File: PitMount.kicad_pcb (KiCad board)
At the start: 2 copper layers, 27 x 30 mm, 16 parts, among them J1 Conn_01x07, Q1 BC817, Q2 IRLML6401, U1 UnifyNano, U2 ELRS-Rx

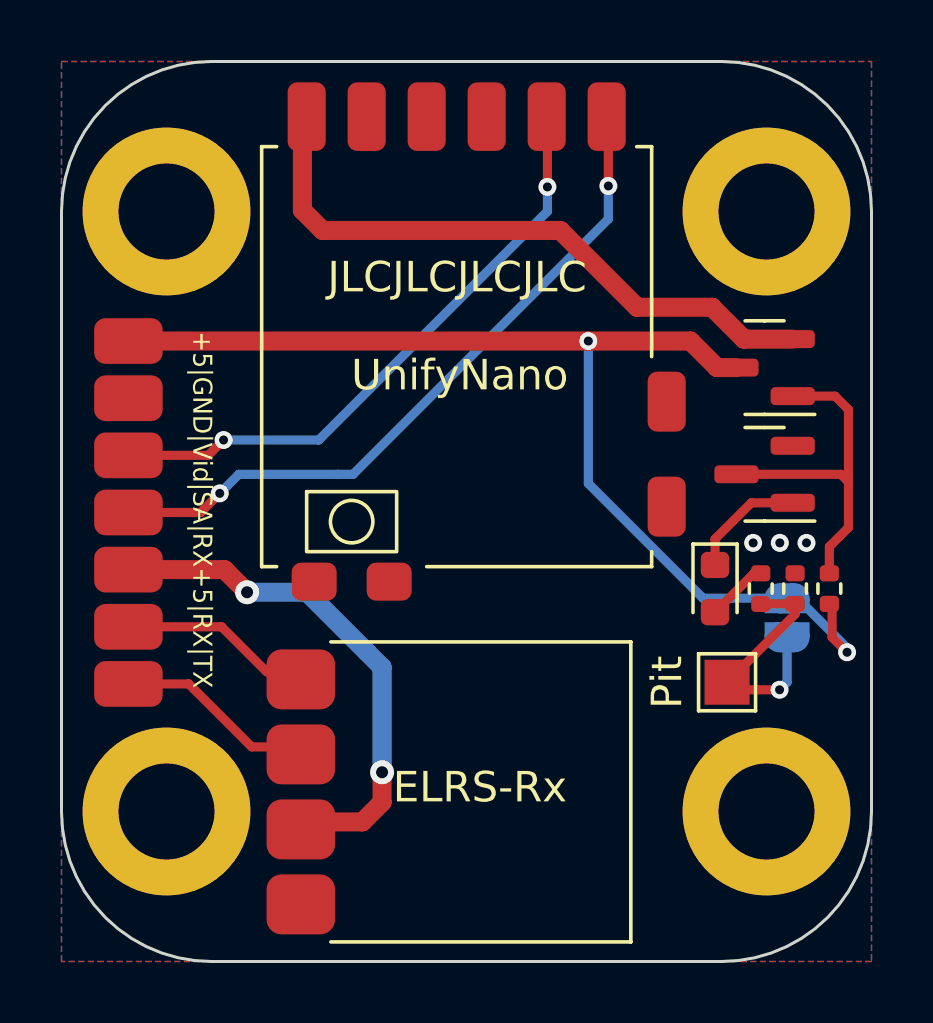
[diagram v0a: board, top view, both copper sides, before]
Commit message: Update PCB with new footprints
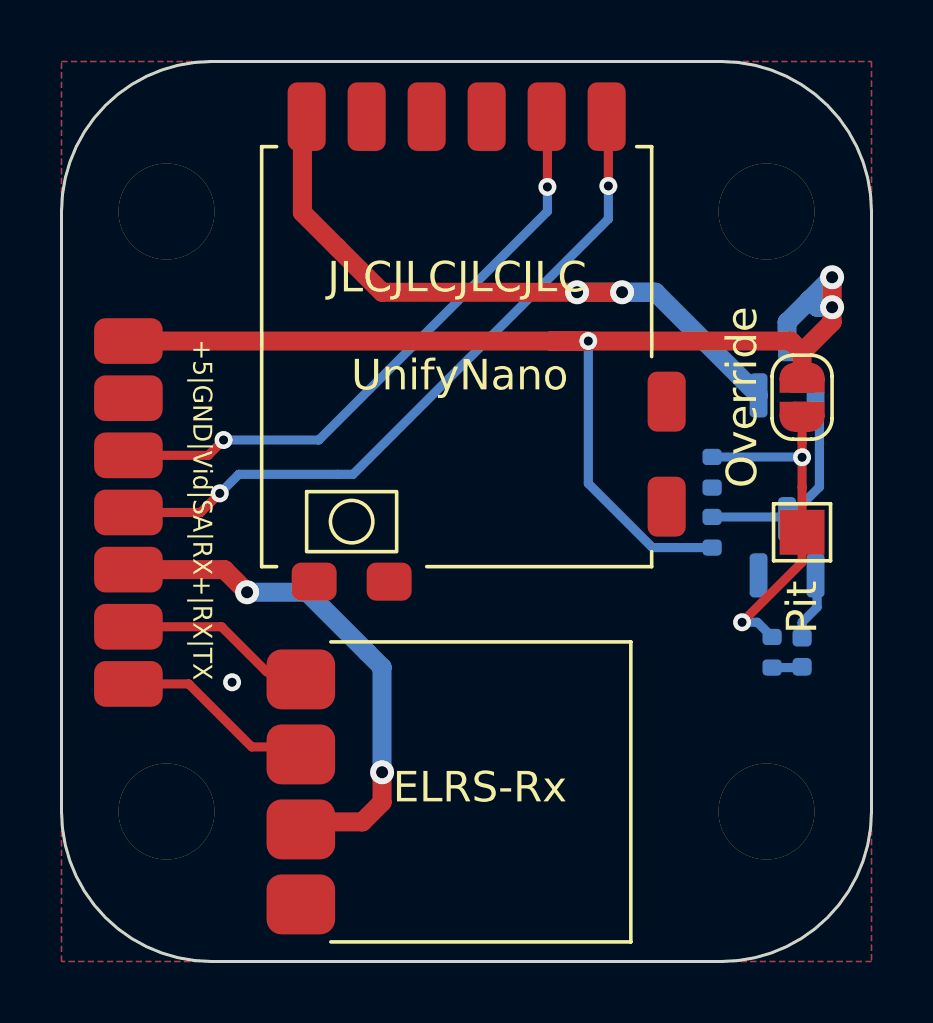
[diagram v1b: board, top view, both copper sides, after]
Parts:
- D1: value 19-217/R6C-P1Q2/3T -> 2SA0402S11A0JT01; footprint LED_SMD:LED_0603_1608Metric -> LED_SMD:LED_0402_1005Metric; moved to B.Cu
- H1, H2, H3, H4: footprint MountingHole:MountingHole_3.2mm_M3_DIN965_Pad -> PitMount:3.2mm_PTH
- JP1: moved to F.Cu
- Q1, Q2, R1, R2, R3: moved to B.Cu
- moved JP1 7.37 mm to (160.0, 97.0)
- moved TP1 5.59 mm to (160.0, 101.5)
- moved R1 4.76 mm to (157.0, 99.5), turned to -90 degrees
- moved R2 4.34 mm to (157.0, 101.5)
- moved D1 3.59 mm to (160.0, 105.5)
- moved Q1 2.55 mm to (159.5, 102.0), turned to 90 degrees
- moved R3 2.16 mm to (159.0, 105.5), turned to -90 degrees
- moved Q2 0.75 mm to (159.5, 96.0), turned to 90 degrees
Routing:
- net Net-(Q1-Pad3): track 11.6 -> 7.16 mm
- net +5V: track 38.3 -> 41.9 mm, vias 2 -> 3
- net Net-(JP1-Pad2): track 8.40 -> 11.9 mm, vias 1 -> 2
- net /VTXPwr: track 21.1 -> 23.4 mm, vias 0 -> 2
- net Net-(D1-Pad1): track 3.95 -> 2.31 mm
- net Net-(D1-Pad2): track 2.06 -> 1.01 mm
- net GND: vias 3 -> 1
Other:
- board text added: "+5|GND|Vid|SA|RX+|RX|TX"
- board text added: "Override"
- board text removed: "+5|GND|Vid|SA|RX+5|RX|TX"

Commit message: Add tooling holes to PCB
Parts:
- added H5: Tooling_Hole, PitMount:Tooling Hole, F.Cu at (141.0, 87.0)
- added H6: Tooling_Hole, PitMount:Tooling Hole, F.Cu at (157.0, 114.5)
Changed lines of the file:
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@@
       ))
+  )
+  (footprint "PitMount:Tooling Hole" (layer "F.Cu")
+    (at 141 87)
+    (property "Sheetfile" "PitMount.kicad_sch")
+    (property "Sheetname" "")
+    (fp_text reference "H5" (at 0 -4.75 unlocked) (layer "F.SilkS") hide
+      (effects (font (size 1 1) (thickness 0.15)))
+    )
+    (fp_text value "Tooling_Hole" (at 0 -3.25 unlocked) (layer "F.Fab")
+      (effects (font (size 1 1) (thickness 0.15)))
+    )
+    (fp_text user "${REFERENCE}" (at 0 -1.75 unlocked) (layer "F.Fab")
+      (effects (font (size 1 1) (thickness 0.15)))
+    )
+    (pad "" np_thru_hole circle (at 0 0) (size 1.152 1.152) (drill 1.152) (layers *.Mask)
+      (solder_mask_margin 0.148) (zone_connect 0))
   )
   (footprint "PitMount:3.2mm_PTH" locked (layer "F.Cu")
@@
       (net 2 "GND") (pinfunction "1") (pintype "input"))
   )
+  (footprint "PitMount:Tooling Hole" (layer "F.Cu")
+    (at 157 114.5)
+    (property "Sheetfile" "PitMount.kicad_sch")
+    (property "Sheetname" "")
+    (fp_text reference "H6" (at 0 -4.75 unlocked) (layer "F.SilkS") hide
+      (effects (font (size 1 1) (thickness 0.15)))
+    )
+    (fp_text value "Tooling_Hole" (at 0 -3.25 unlocked) (layer "F.Fab")
+      (effects (font (size 1 1) (thickness 0.15)))
+    )
+    (fp_text user "${REFERENCE}" (at 0 -1.75 unlocked) (layer "F.Fab")
+      (effects (font (size 1 1) (thickness 0.15)))
+    )
+    (pad "" np_thru_hole circle (at 0 0) (size 1.152 1.152) (drill 1.152) (layers *.Mask)
+      (solder_mask_margin 0.148) (zone_connect 0))
+  )
   (footprint "PitMount:VTXConn" (layer "F.Cu")
